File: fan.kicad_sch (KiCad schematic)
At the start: 0 parts

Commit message: moved over a lot of schematic from the bitaxe
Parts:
- added C1: 470pF, Capacitor_SMD:C_0402_1005Metric, symbol Device:C
- added C2: 220uF, Capacitor_SMD:CP_Elec_6.3x7.7, symbol Device:C_Polarized
- added C3, C4: 311-3342-1-ND, Capacitor_SMD:C_0402_1005Metric, symbol Device:C
- added J2: Conn_01x04, bitaxe:470531000, symbol Connector_Generic:Conn_01x04
- added R1, R2: 100, Resistor_SMD:R_0402_1005Metric, symbol DayMiner-eagle-import:RESISTOR0402-RES
- added R3, R4: 10k, Resistor_SMD:R_0402_1005Metric, symbol Device:R_US
- added TP1, TP2: TestPoint, TestPoint:TestPoint_Pad_D1.5mm, symbol Connector:TestPoint
- added U1: EMC2101, Package_SO:TSSOP-8_3x3mm_P0.65mm, symbol dayminer:EMC2101
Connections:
- new net: C1.1, R2.2, U1.2 (DP)
- new net: C1.2, R1.1, U1.3 (DN)
- new net 3V3: C4.1, R3.2, R4.2, U1.1 (VDD)
- new net 5V: C2.1, C3.1, J2.2 (Pin_2)
- new net FAN_PWM: J2.4 (Pin_4), R4.1, TP2.1, U1.4 (FAN)
- new net FAN_TACH: J2.3 (Pin_3), R3.1, TP1.1, U1.6 (ALERT/TACH)
- new net GND: C2.2, C3.2, C4.2, J2.1 (Pin_1), U1.5 (GND)
- new net SCL: U1.8 (SMCLK)
- new net SDA: U1.7 (SMDATA)
- new net TEMP_N: R1.2
- new net TEMP_P: R2.1
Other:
- note added: "I2C Address: 0x4C"

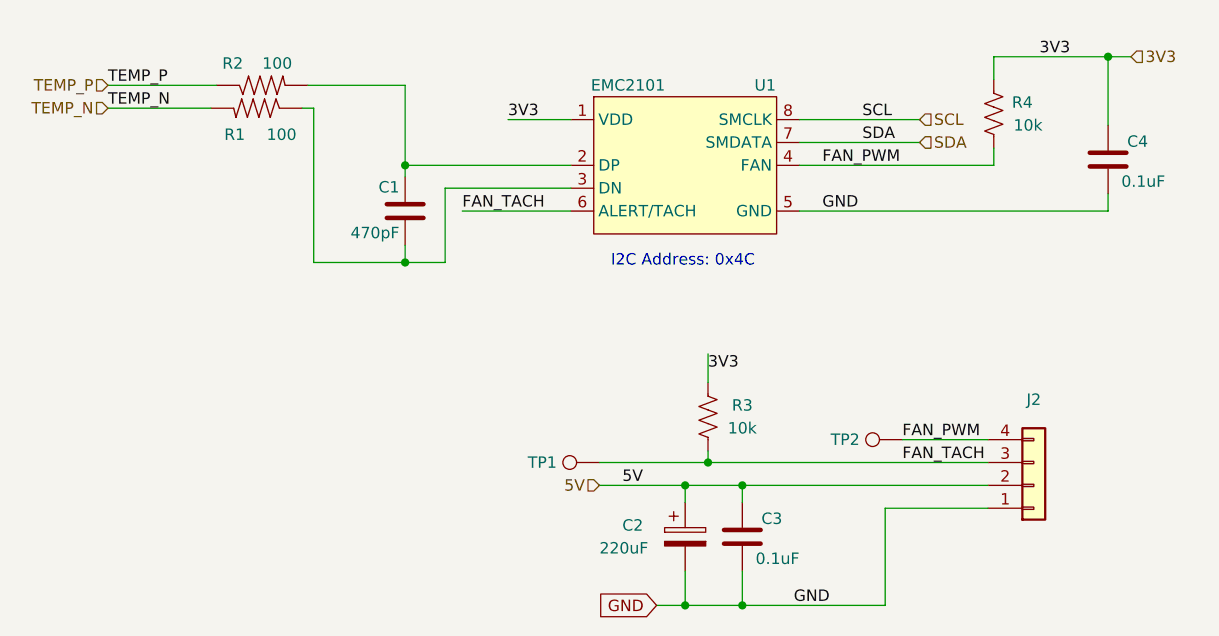
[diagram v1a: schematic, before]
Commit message: cleared up some part reference designator madness
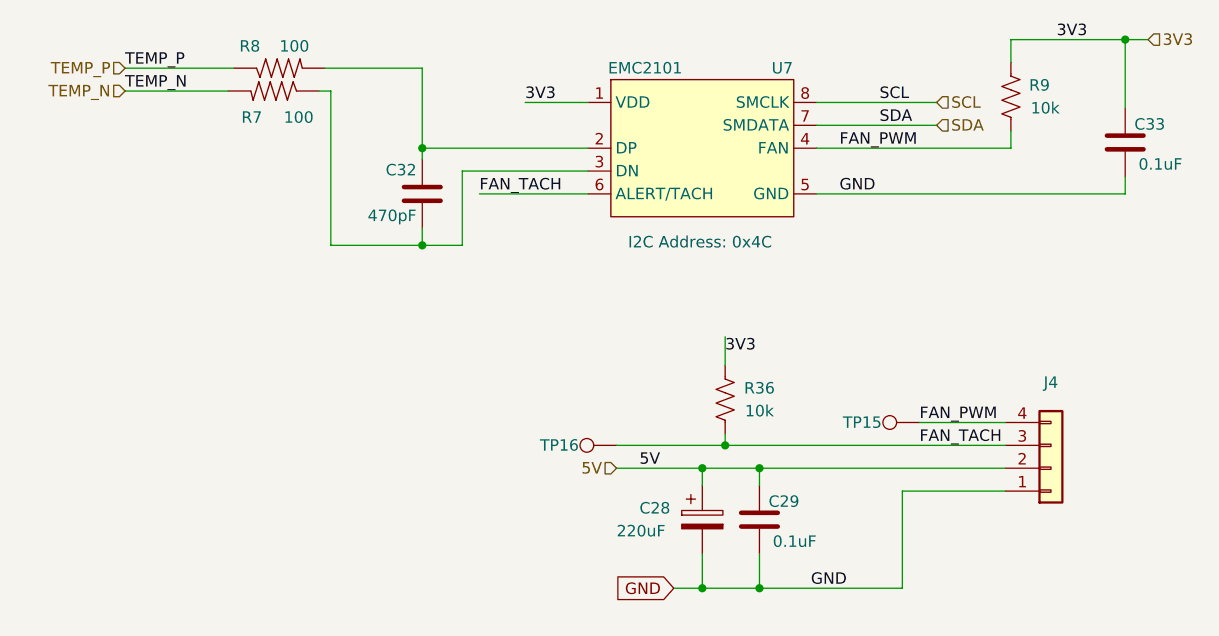
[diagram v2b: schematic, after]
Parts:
- removed C1: 470pF, Capacitor_SMD:C_0402_1005Metric, symbol Device:C
- removed C2: 220uF, Capacitor_SMD:CP_Elec_6.3x7.7, symbol Device:C_Polarized
- removed C3, C4: 311-3342-1-ND, Capacitor_SMD:C_0402_1005Metric, symbol Device:C
- removed J2: Conn_01x04, bitaxe:470531000, symbol Connector_Generic:Conn_01x04
- removed R1, R2: 100, Resistor_SMD:R_0402_1005Metric, symbol DayMiner-eagle-import:RESISTOR0402-RES
- removed R3, R4: 10k, Resistor_SMD:R_0402_1005Metric, symbol Device:R_US
- removed TP1, TP2: TestPoint, TestPoint:TestPoint_Pad_D1.5mm, symbol Connector:TestPoint
- removed U1: EMC2101, Package_SO:TSSOP-8_3x3mm_P0.65mm, symbol dayminer:EMC2101
- added C28: 220uF, Capacitor_SMD:CP_Elec_6.3x7.7, symbol Device:C_Polarized
- added C29, C33: 311-3342-1-ND, Capacitor_SMD:C_0402_1005Metric, symbol Device:C
- added C32: 470pF, Capacitor_SMD:C_0402_1005Metric, symbol Device:C
- added J4: Conn_01x04, bitaxe:470531000, symbol Connector_Generic:Conn_01x04
- added R36, R9: 10k, Resistor_SMD:R_0402_1005Metric, symbol Device:R_US
- added R7, R8: 100, Resistor_SMD:R_0402_1005Metric, symbol DayMiner-eagle-import:RESISTOR0402-RES
- added TP15, TP16: TestPoint, TestPoint:TestPoint_Pad_D1.5mm, symbol Connector:TestPoint
- added U7: EMC2101, Package_SO:TSSOP-8_3x3mm_P0.65mm, symbol dayminer:EMC2101
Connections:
- net 3V3: now also C33.1, R36.2, R9.2, U7.1 (VDD)
- net 5V: now also C28.1, C29.1, J4.2 (Pin_2)
- net FAN_PWM: now also J4.4 (Pin_4), R9.1, TP15.1, U7.4 (FAN)
- net FAN_TACH: now also J4.3 (Pin_3), R36.1, TP16.1, U7.6 (ALERT/TACH)
- net GND: now also C28.2, C29.2, C33.2, J4.1 (Pin_1), U7.5 (GND)
- net SCL: now also U7.8 (SMCLK)
- net SDA: now also U7.7 (SMDATA)
- net TEMP_N: now also R7.2
- net TEMP_P: now also R8.1
- new net: C32.1, R8.2, U7.2 (DP)
- new net: C32.2, R7.1, U7.3 (DN)

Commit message: cleanup. added LCSC fan connector
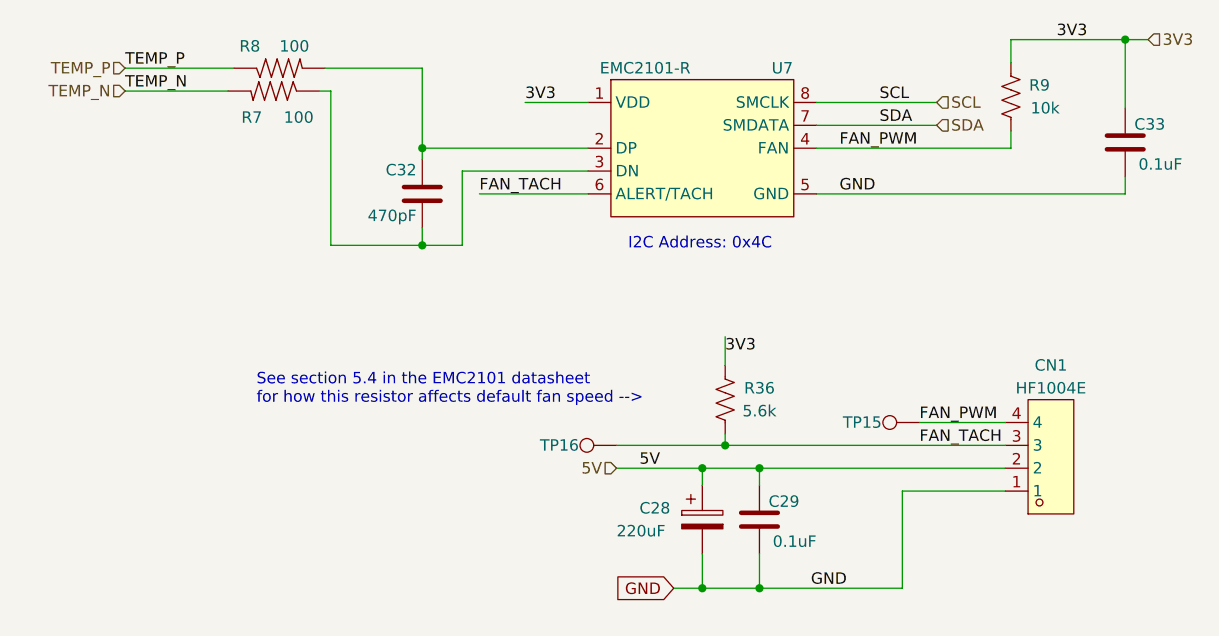
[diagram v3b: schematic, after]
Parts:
- removed J4: Conn_01x04, bitaxe:470531000, symbol Connector_Generic:Conn_01x04
- added CN1: HF1004E, lcsc:CONN-TH_4P-P2.54_A2510S-4P, symbol lcsc:HF1004E
- R36: value 10k -> 5.6k; DK 311-10KJRCT-ND -> (none); PARTNO RC0402JR-0710KL -> (none)
- U7: value EMC2101 -> EMC2101-R
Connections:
- net 5V: now also CN1.2
- net FAN_PWM: now also CN1.4
- net FAN_TACH: now also CN1.3
- net GND: now also CN1.1
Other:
- note added: "See section 5.4 in the EMC2101 datasheet for how this resistor affects default fan speed -->"
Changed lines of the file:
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@@
     (stroke (width 0) (type default))
+  )
+  (text "See section 5.4 in the EMC2101 datasheet \nfor how this resistor affects default fan speed -->"
+    (at 97.79 95.885 0)
+    (effects (font (size 1.27 1.27)) (justify left bottom))
   )
   (text "I2C Address: 0x4C" (at 139.065 78.74 0)
@@
     )
   )
+  (symbol (lib_id "lcsc:HF1004E") (at 186.055 101.6 0) (mirror x) (unit 1)
+    (in_bom yes) (on_board yes) (dnp no) (fields_autoplaced)
+    (property "Reference" "CN1" (at 186.055 91.44 0)
+      (effects (font (size 1.27 1.27)))
+    )
+    (property "Value" "HF1004E" (at 186.055 93.98 0)
+      (effects (font (size 1.27 1.27)))
+    )
+    (property "Footprint" "lcsc:CONN-TH_4P-P2.54_A2510S-4P" (at 186.055 90.17 0)
+      (effects (font (size 1.27 1.27)) hide)
+    )
+    (property "Datasheet" "" (at 186.055 101.6 0)
+      (effects (font (size 1.27 1.27)) hide)
+    )
+    (property "Manufacturer" "FOXCONN(富士康)" (at 186.055 87.63 0)
+      (effects (font (size 1.27 1.27)) hide)
+    )
+    (property "LCSC Part" "C2761402" (at 186.055 85.09 0)
+      (effects (font (size 1.27 1.27)) hide)
+    )
+    (property "JLC Part" "Extended Part" (at 186.055 82.55 0)
+      (effects (font (size 1.27 1.27)) hide)
+    )
+    (pin "1")
+    (pin "2")
+    (pin "3")
+    (pin "4")
+    (instances
+      (project "Hashat"
+        (path "/00740941-7ad8-466a-a267-188591e2b5c4/d3bb94e0-7d79-4528-af92-86eea189a8bc"
+          (reference "CN1") (unit 1)
+        )
+      )
+    )
+  )
   (symbol (lib_id "Device:C") (at 194.31 66.675 0) (mirror y) (unit 1)
     (in_bom yes) (on_board yes) (dnp no)
@@
       (effects (font (size 1.27 1.27)))
     )
-    (property "Value" "EMC2101" (at 140.97 58.42 0)
+    (property "Value" "EMC2101-R" (at 140.97 58.42 0)
       (effects (font (size 1.27 1.27)))
     )
@@
     )
   )
-  (symbol (lib_id "Connector_Generic:Conn_01x04") (at 186.055 102.87 0) (mirror x) (unit 1)
-    (in_bom yes) (on_board yes) (dnp no) (fields_autoplaced)
-    (property "Reference" "J4" (at 186.055 93.345 0)
-      (effects (font (size 1.27 1.27)))
-    )
-    (property "Value" "Conn_01x04" (at 186.055 93.345 0)
-      (effects (font (size 1.27 1.27)) hide)
-    )
-    (property "Footprint" "bitaxe:470531000" (at 186.055 102.87 0)
-      (effects (font (size 1.27 1.27)) hide)
-    )
-    (property "Datasheet" "~" (at 186.055 102.87 0)
-      (effects (font (size 1.27 1.27)) hide)
-    )
-    (property "PARTNO" "0470531000" (at 186.055 102.87 0)
-      (effects (font (size 1.27 1.27)) hide)
-    )
-    (property "DK" "WM4330-ND" (at 186.055 102.87 0)
-      (effects (font (size 1.27 1.27)) hide)
-    )
-    (pin "1")
-    (pin "2")
-    (pin "3")
-    (pin "4")
-    (instances
-      (project "Hashat"
-        (path "/00740941-7ad8-466a-a267-188591e2b5c4/d3bb94e0-7d79-4528-af92-86eea189a8bc"
-          (reference "J4") (unit 1)
-        )
-      )
-      (project "bitaxeMax"
-        (path "/e63e39d7-6ac0-4ffd-8aa3-1841a4541b55/8e8832ea-6bf1-49d2-b3a5-32a207f555d2"
-          (reference "J4") (unit 1)
-        )
-      )
-    )
-  )
   (symbol (lib_id "Connector:TestPoint") (at 137.795 100.33 90) (mirror x) (unit 1)
     (in_bom yes) (on_board yes) (dnp no)
@@
       (effects (font (size 1.27 1.27)))
     )
-    (property "Value" "10k" (at 153.67 96.52 0)
+    (property "Value" "5.6k" (at 153.67 96.52 0)
       (effects (font (size 1.27 1.27)))
     )
@@
       (effects (font (size 1.27 1.27)) hide)
     )
-    (property "DK" "311-10KJRCT-ND" (at 149.86 95.25 0)
-      (effects (font (size 1.27 1.27)) hide)
-    )
-    (property "PARTNO" "RC0402JR-0710KL" (at 149.86 95.25 0)
-      (effects (font (size 1.27 1.27)) hide)
-    )
+    (property "DK" "" (at 149.86 95.25 0)
+      (effects (font (size 1.27 1.27)) hide)
+    )
+    (property "PARTNO" "" (at 149.86 95.25 0)
+      (effects (font (size 1.27 1.27)) hide)
+    )

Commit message: started on new LM5085 based buck design
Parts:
- U7: LCSC Part (none) -> C626968
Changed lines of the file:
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@@
+      (effects (font (size 1.27 1.27)) hide)
+    )
+    (property "LCSC Part" "C626968" (at 147.32 67.31 0)
       (effects (font (size 1.27 1.27)) hide)
     )

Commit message: more routing
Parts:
- removed CN1: HF1004E, lcsc:CONN-TH_4P-P2.54_A2510S-4P, symbol lcsc:HF1004E
- added J2: Conn_01x04, Connector_PinHeader_2.54mm:PinHeader_1x04_P2.54mm_Vertical, symbol Connector_Generic:Conn_01x04
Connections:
- net 5V: now also J2.2 (Pin_2)
- net FAN_PWM: now also J2.4 (Pin_4)
- net FAN_TACH: now also J2.3 (Pin_3)
- net GND: now also J2.1 (Pin_1)
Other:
- note added: "See table 4-1 in the EMC2101 datasheet for how this resistor affects default fan speed -->"
- note removed: "See section 5.4 in the EMC2101 datasheet for how this resistor affects default fan speed -->"
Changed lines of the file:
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@@
     (stroke (width 0) (type default))
   )
-  (text "See section 5.4 in the EMC2101 datasheet \nfor how this resistor affects default fan speed -->"
+  (text "See table 4-1 in the EMC2101 datasheet \nfor how this resistor affects default fan speed -->"
     (at 97.79 95.885 0)
     (effects (font (size 1.27 1.27)) (justify left bottom))
@@
         (path "/e63e39d7-6ac0-4ffd-8aa3-1841a4541b55/8e8832ea-6bf1-49d2-b3a5-32a207f555d2"
           (reference "TP15") (unit 1)
-        )
-      )
-    )
-  )
-  (symbol (lib_id "lcsc:HF1004E") (at 186.055 101.6 0) (mirror x) (unit 1)
-    (in_bom yes) (on_board yes) (dnp no) (fields_autoplaced)
-    (property "Reference" "CN1" (at 186.055 91.44 0)
-      (effects (font (size 1.27 1.27)))
-    )
-    (property "Value" "HF1004E" (at 186.055 93.98 0)
-      (effects (font (size 1.27 1.27)))
-    )
-    (property "Footprint" "lcsc:CONN-TH_4P-P2.54_A2510S-4P" (at 186.055 90.17 0)
-      (effects (font (size 1.27 1.27)) hide)
-    )
-    (property "Datasheet" "" (at 186.055 101.6 0)
-      (effects (font (size 1.27 1.27)) hide)
-    )
-    (property "Manufacturer" "FOXCONN(富士康)" (at 186.055 87.63 0)
-      (effects (font (size 1.27 1.27)) hide)
-    )
-    (property "LCSC Part" "C2761402" (at 186.055 85.09 0)
-      (effects (font (size 1.27 1.27)) hide)
-    )
-    (property "JLC Part" "Extended Part" (at 186.055 82.55 0)
-      (effects (font (size 1.27 1.27)) hide)
-    )
-    (pin "1")
-    (pin "2")
-    (pin "3")
-    (pin "4")
-    (instances
-      (project "Hashat"
-        (path "/00740941-7ad8-466a-a267-188591e2b5c4/d3bb94e0-7d79-4528-af92-86eea189a8bc"
-          (reference "CN1") (unit 1)
         )
       )
@@
         )
       )
+    )
+  )
+  (symbol (lib_id "Connector_Generic:Conn_01x04") (at 186.055 102.87 0) (mirror x) (unit 1)
+    (in_bom yes) (on_board yes) (dnp no) (fields_autoplaced)
+    (property "Reference" "J2" (at 186.055 95.25 0)
+      (effects (font (size 1.27 1.27)))
+    )
+    (property "Value" "Conn_01x04" (at 186.055 94.615 0)
+      (effects (font (size 1.27 1.27)) hide)
+    )
+    (property "Footprint" "Connector_PinHeader_2.54mm:PinHeader_1x04_P2.54mm_Vertical" (at 186.055 102.87 0)
+      (effects (font (size 1.27 1.27)) hide)
+    )
+    (property "Datasheet" "~" (at 186.055 102.87 0)
+      (effects (font (size 1.27 1.27)) hide)
+    )
+    (pin "1")
+    (pin "2")
+    (pin "3")
+    (pin "4")
+    (instances
+      (project "Hashat"
+        (path "/00740941-7ad8-466a-a267-188591e2b5c4/d3bb94e0-7d79-4528-af92-86eea189a8bc"
+          (reference "J2") (unit 1)
+        )
+      )

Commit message: added initial BOM
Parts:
- R36: DK (none) -> 13-RC0402FR-135K6LCT-ND; PARTNO (none) -> RC0402FR-135K6L
- TP15, TP16: now left out of the parts list
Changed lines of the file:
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@@
   )
   (symbol (lib_id "Connector:TestPoint") (at 171.45 97.79 90) (mirror x) (unit 1)
-    (in_bom yes) (on_board yes) (dnp no)
+    (in_bom no) (on_board yes) (dnp no)
     (property "Reference" "TP15" (at 165.1 97.79 90)
       (effects (font (size 1.27 1.27)))
@@
   )
   (symbol (lib_id "Connector:TestPoint") (at 137.795 100.33 90) (mirror x) (unit 1)
-    (in_bom yes) (on_board yes) (dnp no)
+    (in_bom no) (on_board yes) (dnp no)
     (property "Reference" "TP16" (at 131.445 100.33 90)
       (effects (font (size 1.27 1.27)))
@@
       (effects (font (size 1.27 1.27)) hide)
     )
-    (property "DK" "" (at 149.86 95.25 0)
-      (effects (font (size 1.27 1.27)) hide)
-    )
-    (property "PARTNO" "" (at 149.86 95.25 0)
-      (effects (font (size 1.27 1.27)) hide)
-    )
+    (property "DK" "13-RC0402FR-135K6LCT-ND" (at 149.86 95.25 0)
+      (effects (font (size 1.27 1.27)) hide)
+    )
+    (property "PARTNO" "RC0402FR-135K6L" (at 149.86 95.25 0)
+      (effects (font (size 1.27 1.27)) hide)
+    )
